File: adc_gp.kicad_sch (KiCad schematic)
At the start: 69 parts

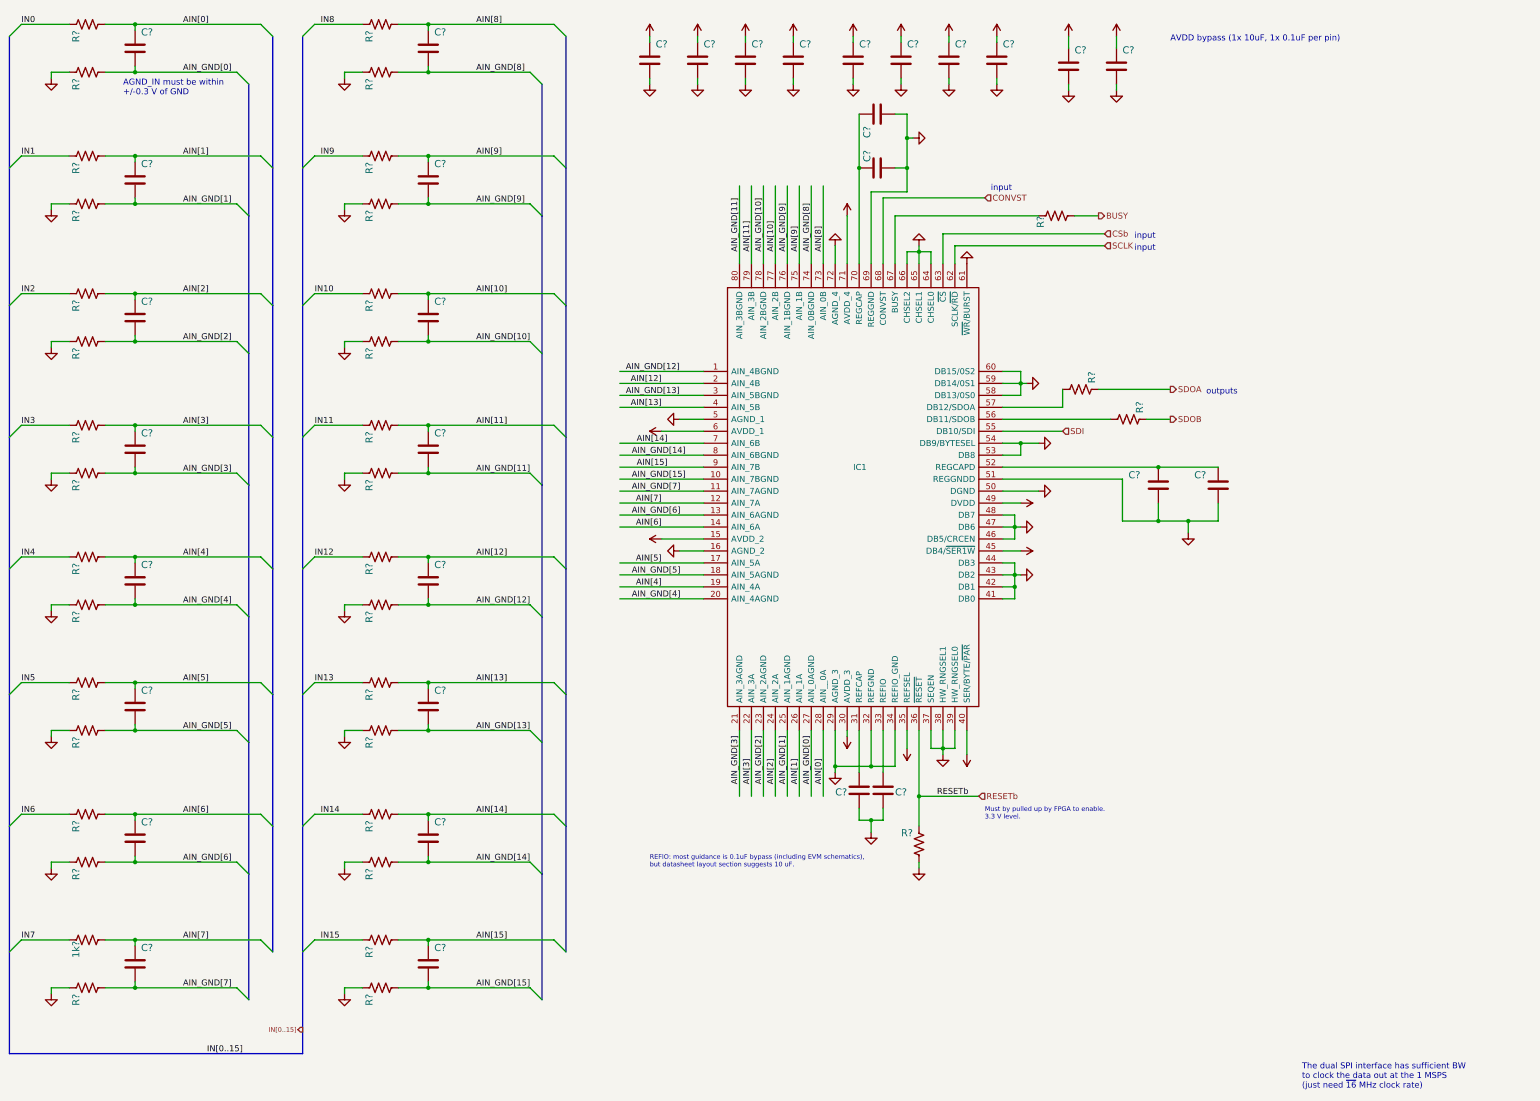
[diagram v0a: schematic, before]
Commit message: closes #31 - incorrect text on Howland current pump. Also, updated fast DAC symbol but not closing until layout is corrected
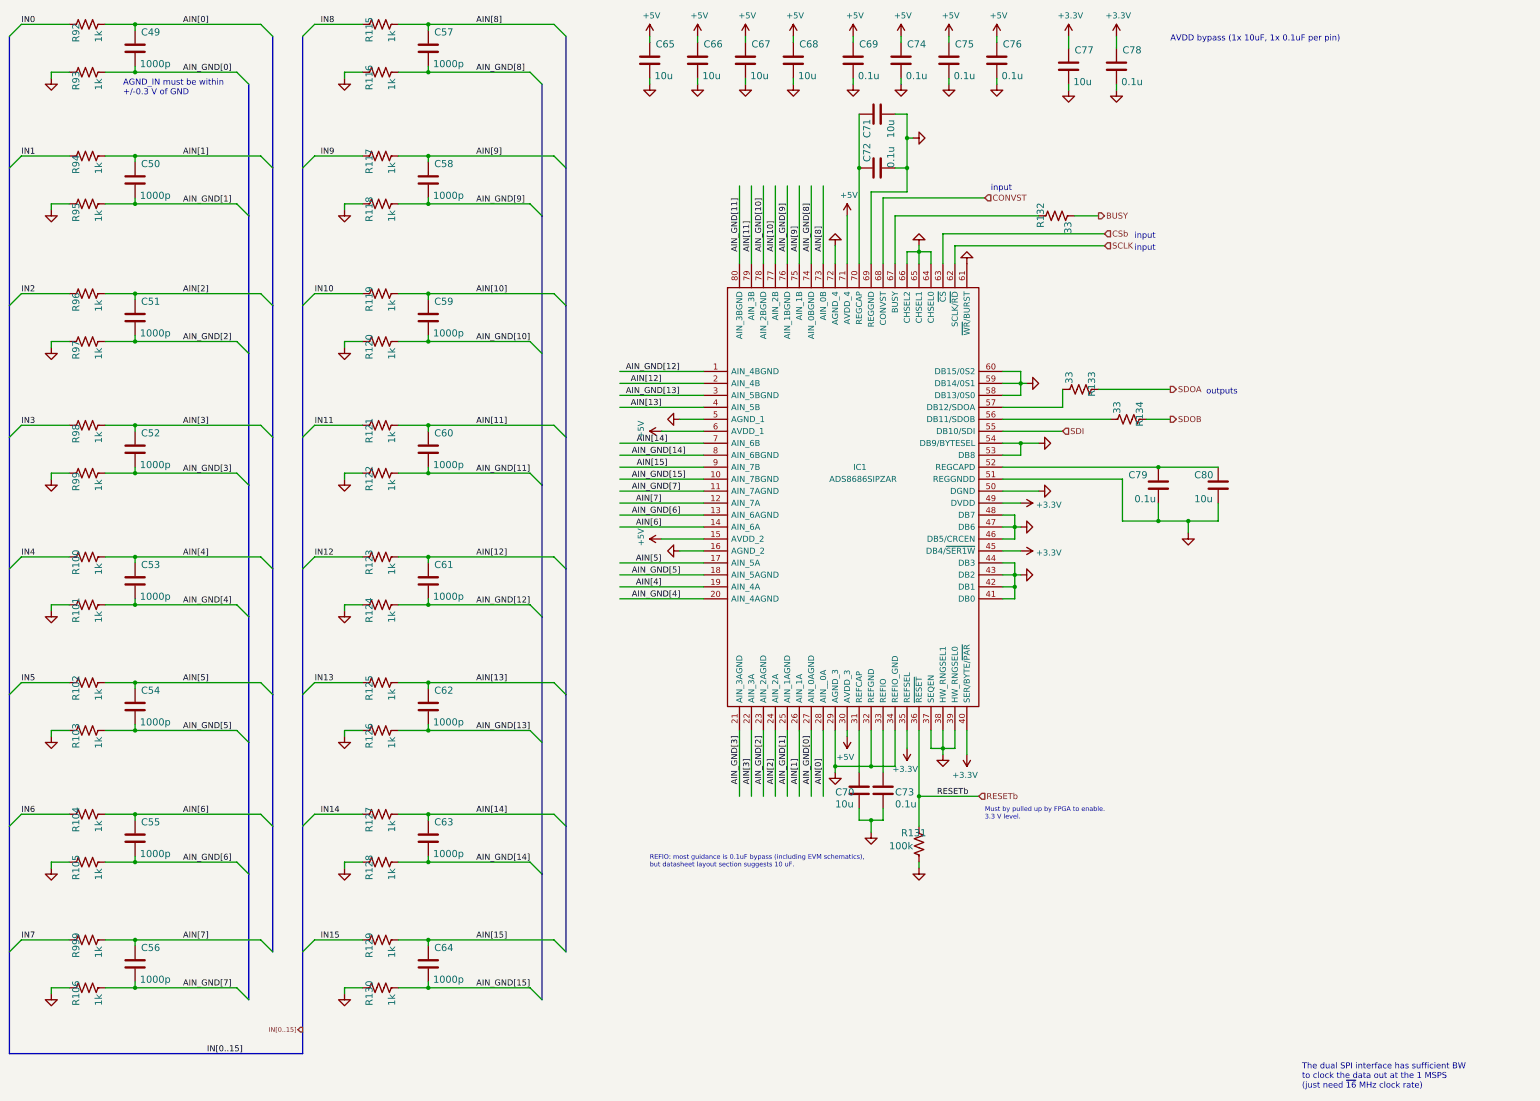
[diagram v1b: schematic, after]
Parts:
- C49, C50, C51, C52, C53, C54, C55, C56, C57, C58, C59, C60, C61, C62, C63, C64: renamed from C?; value (none) -> 1000p; footprint (none) -> Capacitor_SMD:C_0603_1608Metric
- C65, C66, C67, C68, C77: renamed from C?; value (none) -> 10u; footprint (none) -> Capacitor_SMD:C_0603_1608Metric
- C69, C72, C73, C74, C75, C76, C78, C79: renamed from C?; value (none) -> 0.1u; footprint (none) -> Capacitor_SMD:C_0603_1608Metric
- C70, C71, C80: renamed from C?; value (none) -> 10u; footprint (none) -> Capacitor_SMD:C_0805_2012Metric
- IC1: value (none) -> ADS8686SIPZAR; footprint (none) -> Package_QFP:LQFP-80_14x14mm_P0.65mm
- R100, R101, R102, R103, R104, R105, R106, R115, R116, R117, R118, R119, R120, R121, R122, R123, R124, R125, R126, R127, R128, R129, R130, R92, R93, R94, R95, R96, R97, R98, R99: renamed from R?; value (none) -> 1k; footprint (none) -> Resistor_SMD:R_0603_1608Metric
- R131: renamed from R?; value (none) -> 100k; footprint (none) -> Resistor_SMD:R_0603_1608Metric
- R132, R133, R134: renamed from R?; value (none) -> 33; footprint (none) -> Resistor_SMD:R_0603_1608Metric
- R999: renamed from 1k?; value (none) -> 1k; footprint (none) -> Resistor_SMD:R_0603_1608Metric

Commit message: added fast DAC output capacitor of 2.4nF and removed filtering caps at ADS8686 input. Closes #22 and Closes #24
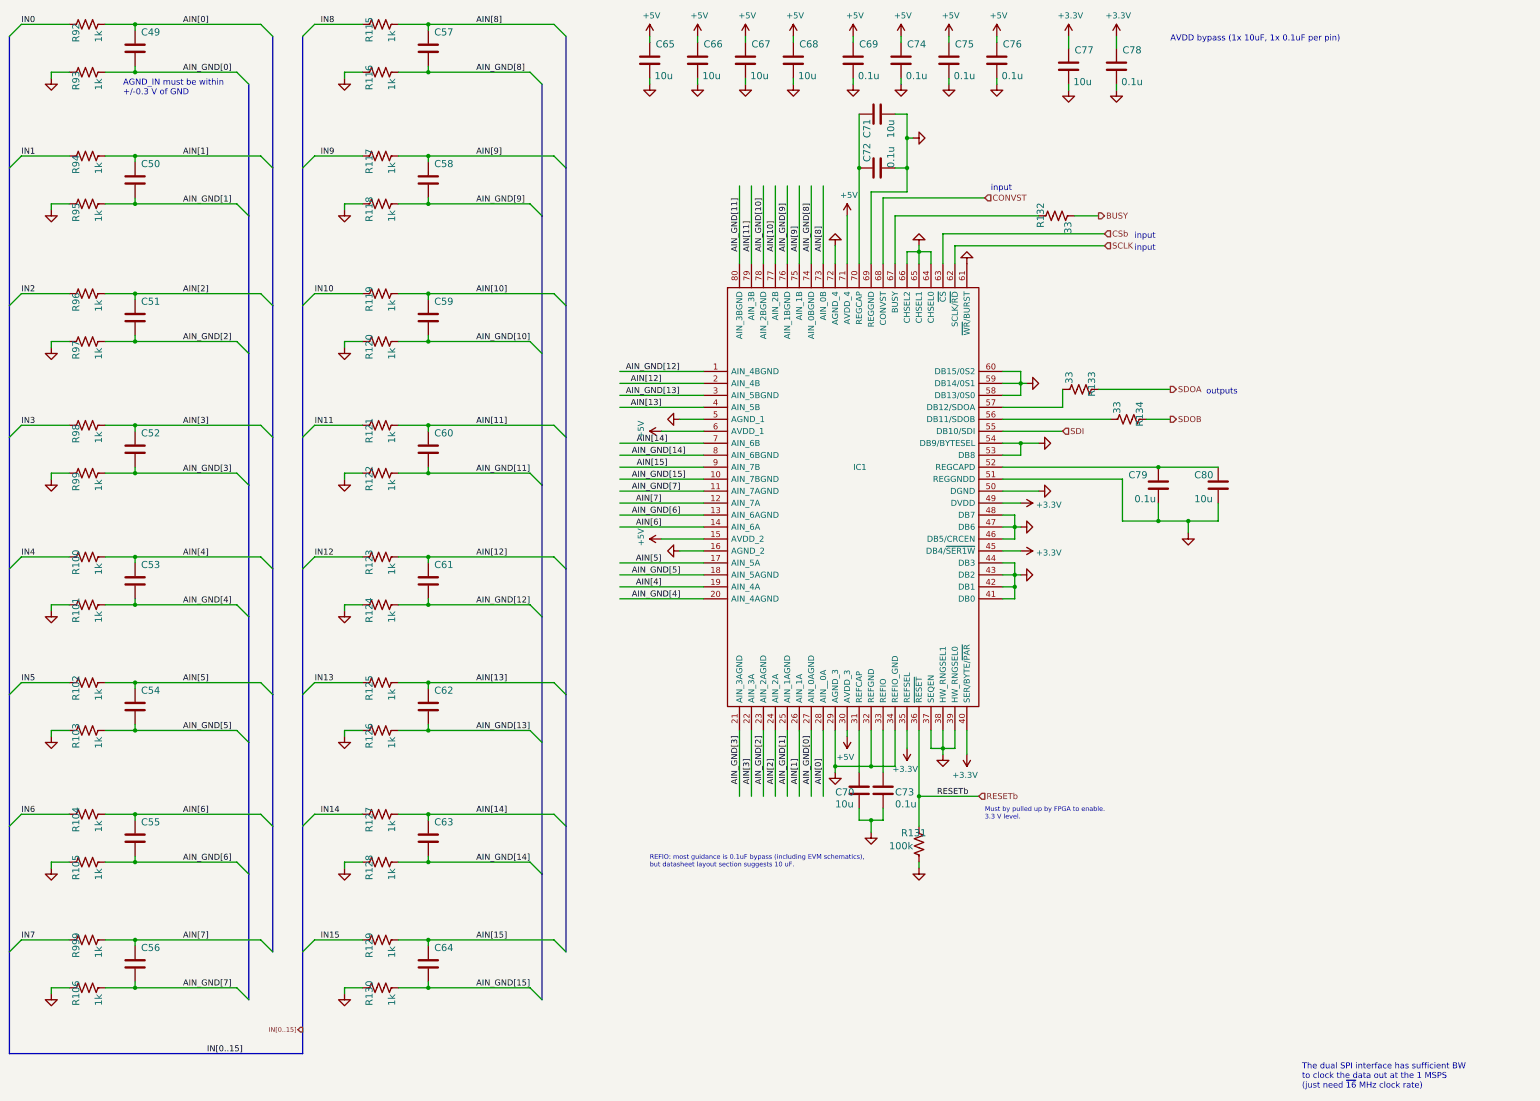
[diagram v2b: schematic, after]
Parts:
- C49, C50, C51, C52, C53, C54, C55, C56, C57, C58, C59, C60, C61, C62, C63, C64: value 1000p -> (none); footprint Capacitor_SMD:C_0603_1608Metric -> (none); Manf# CC0603JRNPO9BN102 -> (none)
- IC1: value ADS8686SIPZAR -> (none); footprint Package_QFP:LQFP-80_14x14mm_P0.65mm -> (none)
